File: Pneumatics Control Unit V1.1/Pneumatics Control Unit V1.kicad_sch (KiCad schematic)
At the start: 50 parts, among them J3 RX_PORT, U2 SN65HVD1782D, U3 FT2232D, Y1 Resonator_Small

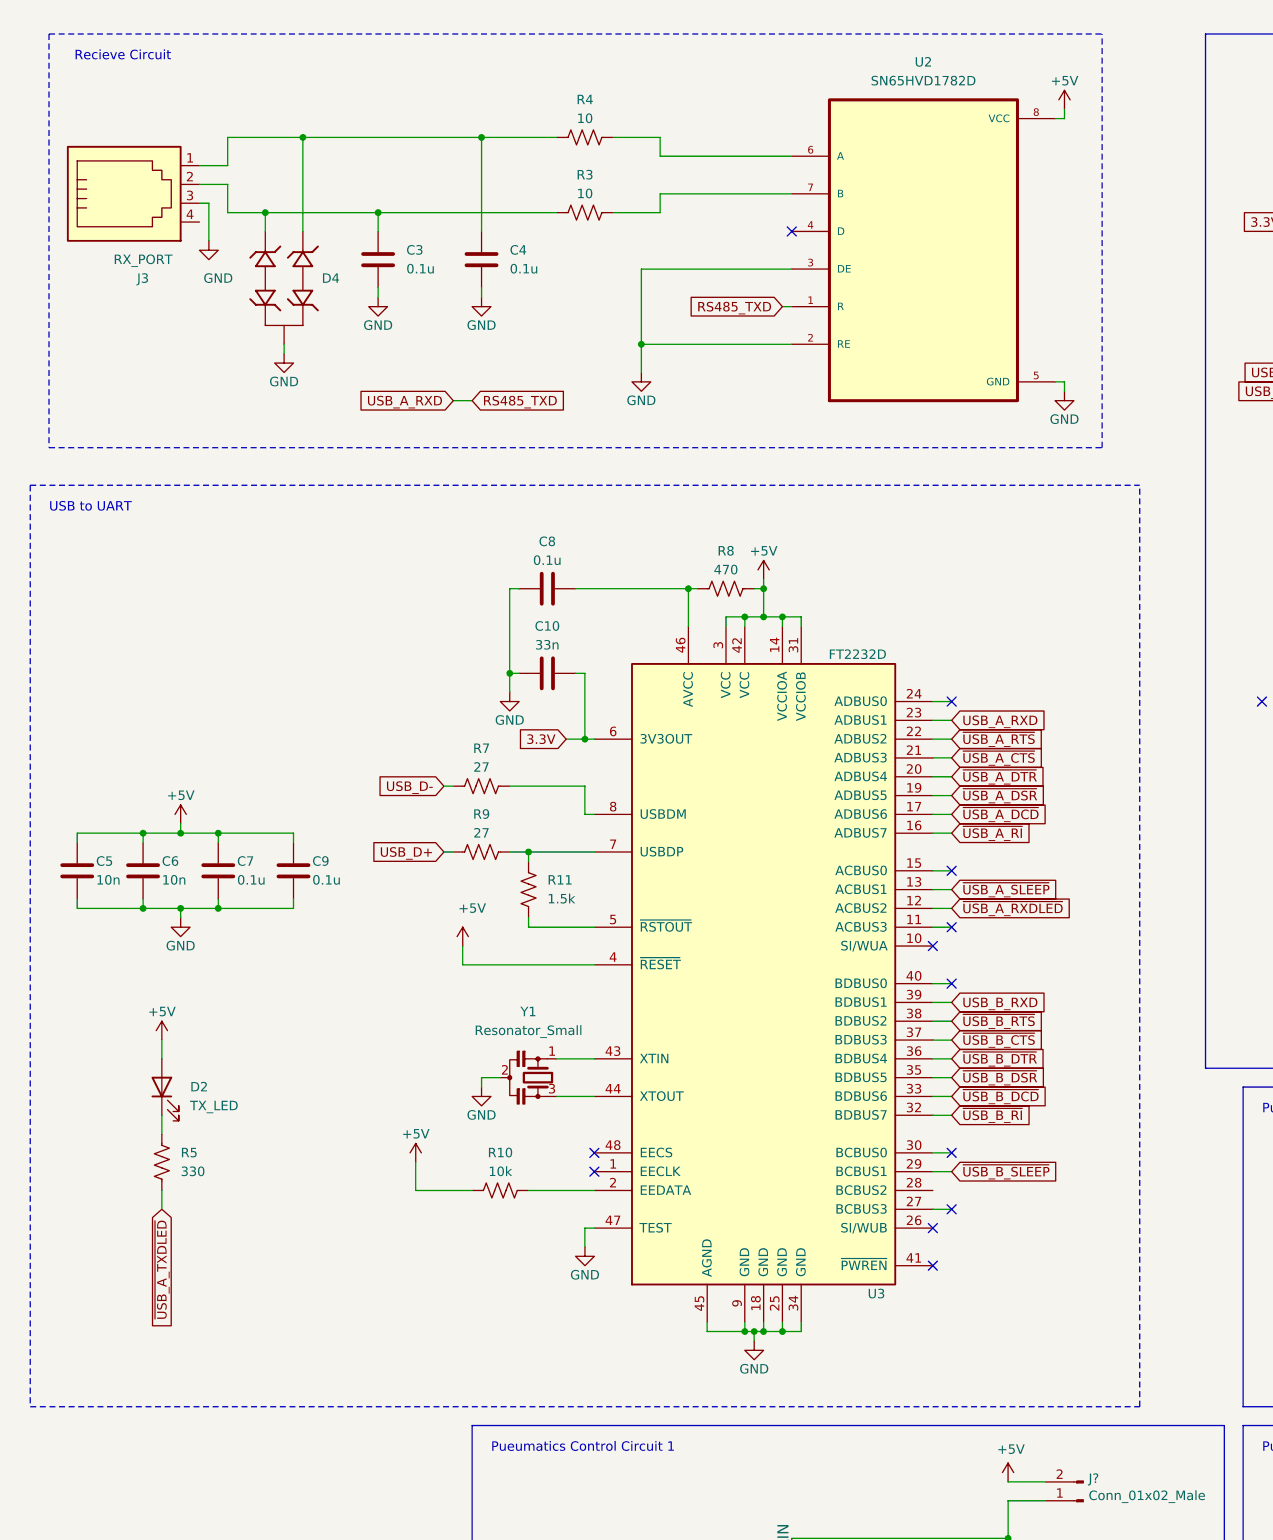
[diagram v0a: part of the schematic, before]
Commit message: using a new chip for RS485 to UART
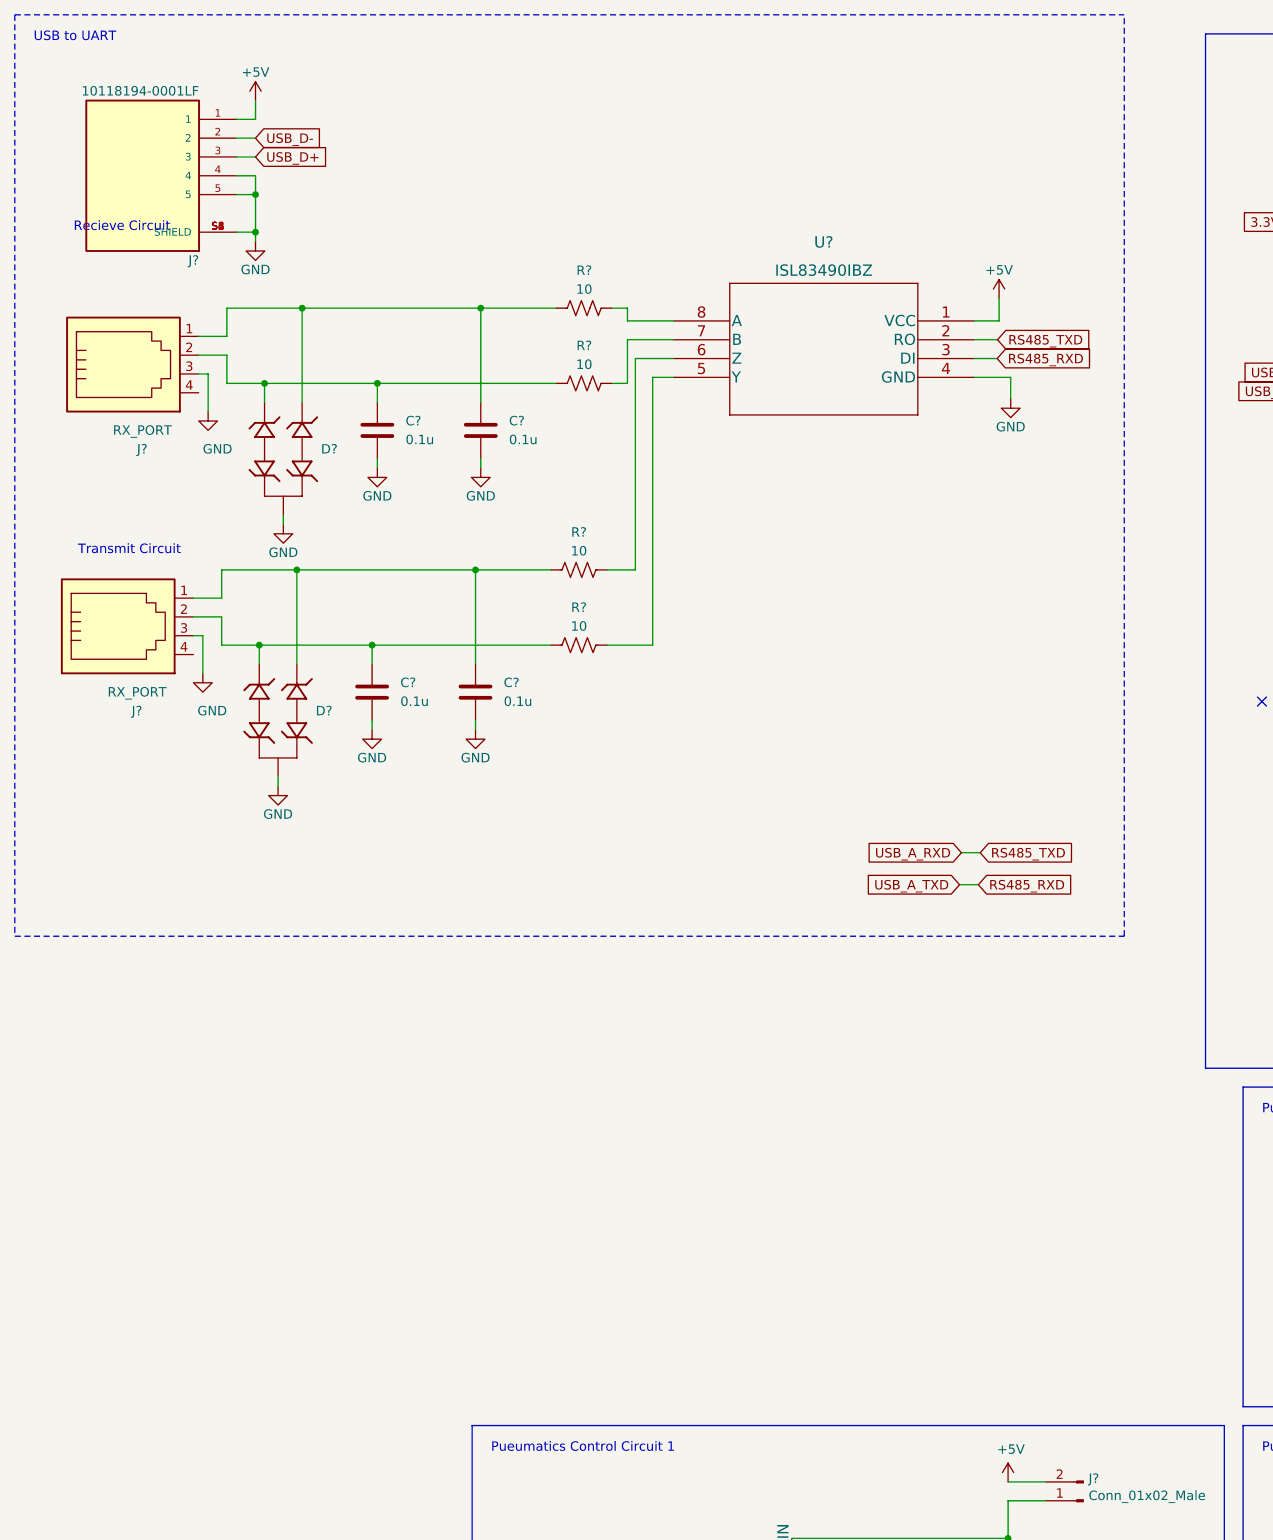
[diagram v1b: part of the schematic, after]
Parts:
- removed C10: 33n, Capacitor_SMD:C_0805_2012Metric_Pad1.18x1.45mm_HandSolder, symbol Device:C
- removed C3, C4, C7, C8, C9: 0.1u, Capacitor_SMD:C_0805_2012Metric_Pad1.18x1.45mm_HandSolder, symbol Device:C
- removed C5, C6: 10n, Capacitor_SMD:C_0805_2012Metric_Pad1.18x1.45mm_HandSolder, symbol Device:C
- removed D2: TX_LED, LED_SMD:LED_0805_2012Metric_Pad1.15x1.40mm_HandSolder, symbol Device:LED
- removed D4: CDSOT23-SM712, CDSOT23-SM712:SOT-23-3, symbol CDSOT23-SM712:CDSOT23-SM712
- removed J3: RX_PORT, Andrew_Custom:C189737, symbol Connector:4P4C
- removed R10: 10k, Resistor_SMD:R_0805_2012Metric_Pad1.20x1.40mm_HandSolder, symbol Device:R_US
- removed R11: 1.5k, Resistor_SMD:R_0805_2012Metric_Pad1.20x1.40mm_HandSolder, symbol Device:R_US
- removed R3, R4: 10, Resistor_SMD:R_0805_2012Metric_Pad1.20x1.40mm_HandSolder, symbol Device:R_US
- removed R5: 330, Resistor_SMD:R_0805_2012Metric_Pad1.20x1.40mm_HandSolder, symbol Device:R_US
- removed R7, R9: 27, Resistor_SMD:R_0805_2012Metric_Pad1.20x1.40mm_HandSolder, symbol Device:R_US
- removed R8: 470, Resistor_SMD:R_0805_2012Metric_Pad1.20x1.40mm_HandSolder, symbol Device:R_US
- removed U2: SN65HVD1782D, SN65HVD1782D:SOIC127P599X175-8N, symbol SN65HVD1782D:SN65HVD1782D
- removed U3: FT2232D, Package_QFP:LQFP-48_7x7mm_P0.5mm, symbol Interface_USB:FT2232D
- removed Y1: Resonator_Small, OSC_CSTCE16M0V53-R0:OSC_CSTCE16M0V53-R0, symbol Device:Resonator_Small
- added C? (x4): 0.1u, Capacitor_SMD:C_0805_2012Metric_Pad1.18x1.45mm_HandSolder, symbol Device:C
- added D? (x2): CDSOT23-SM712, CDSOT23-SM712:SOT-23-3, symbol CDSOT23-SM712:CDSOT23-SM712
- added J? (x2): RX_PORT, Andrew_Custom:C189737, symbol Connector:4P4C
- added J?: 10118194-0001LF, 10118194-0001LF:AMPHENOL_10118194-0001LF, symbol 10118194-0001LF:10118194-0001LF
- added R? (x4): 10, Resistor_SMD:R_0805_2012Metric_Pad1.20x1.40mm_HandSolder, symbol Device:R_US
- added U?: ISL83490IBZ, SOIC8_4X5_INR, symbol 2022-03-23_15-47-26:ISL83490IBZ
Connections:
- net +5V: now also J?.1, U?.1 (VCC)
- net GND: now also C?.2, C?.2, C?.2, C?.2, D?.3, D?.3, J?.3, J?.3, J?.4, J?.5, J?.S1 (SHIELD), J?.S2 (SHIELD), J?.S3 (SHIELD), J?.S4 (SHIELD), J?.S5 (SHIELD), J?.S6 (SHIELD), U?.4 (GND)
- net RS485_TXD: now also U?.2 (RO)
- net USB_D+: now also J?.3
- net USB_D-: now also J?.2
- new net: R?.2, U?.5 (Y)
- new net: R?.2, U?.6 (Z)
- new net: R?.2, U?.7 (B)
- new net: R?.2, U?.8 (A)
- new net: C?.1, D?.2, J?.1, R?.1 (x2)
- new net: C?.1, D?.1, J?.2, R?.1 (x2)
- new net RS485_RXD: U?.3 (DI)
- no-connect marks 56 -> 44
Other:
- note added: "Transmit Circuit"

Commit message: Cleaning up the schematic
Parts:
- removed J?: 10118194-0001LF, 10118194-0001LF:AMPHENOL_10118194-0001LF, symbol 10118194-0001LF:10118194-0001LF
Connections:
- net RS485_RXD: now also J?.17 (TX1)
- net RS485_TXD: now also J?.19 (RX1)
- no-connect marks 44 -> 42
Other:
- note added: "RS485 to UART"
- note removed: "Recieve Circuit"
- note removed: "USB to UART"
- moved on the sheet: C?, D?, H1, H2, H3, J?, MOSFET?, R?, U?

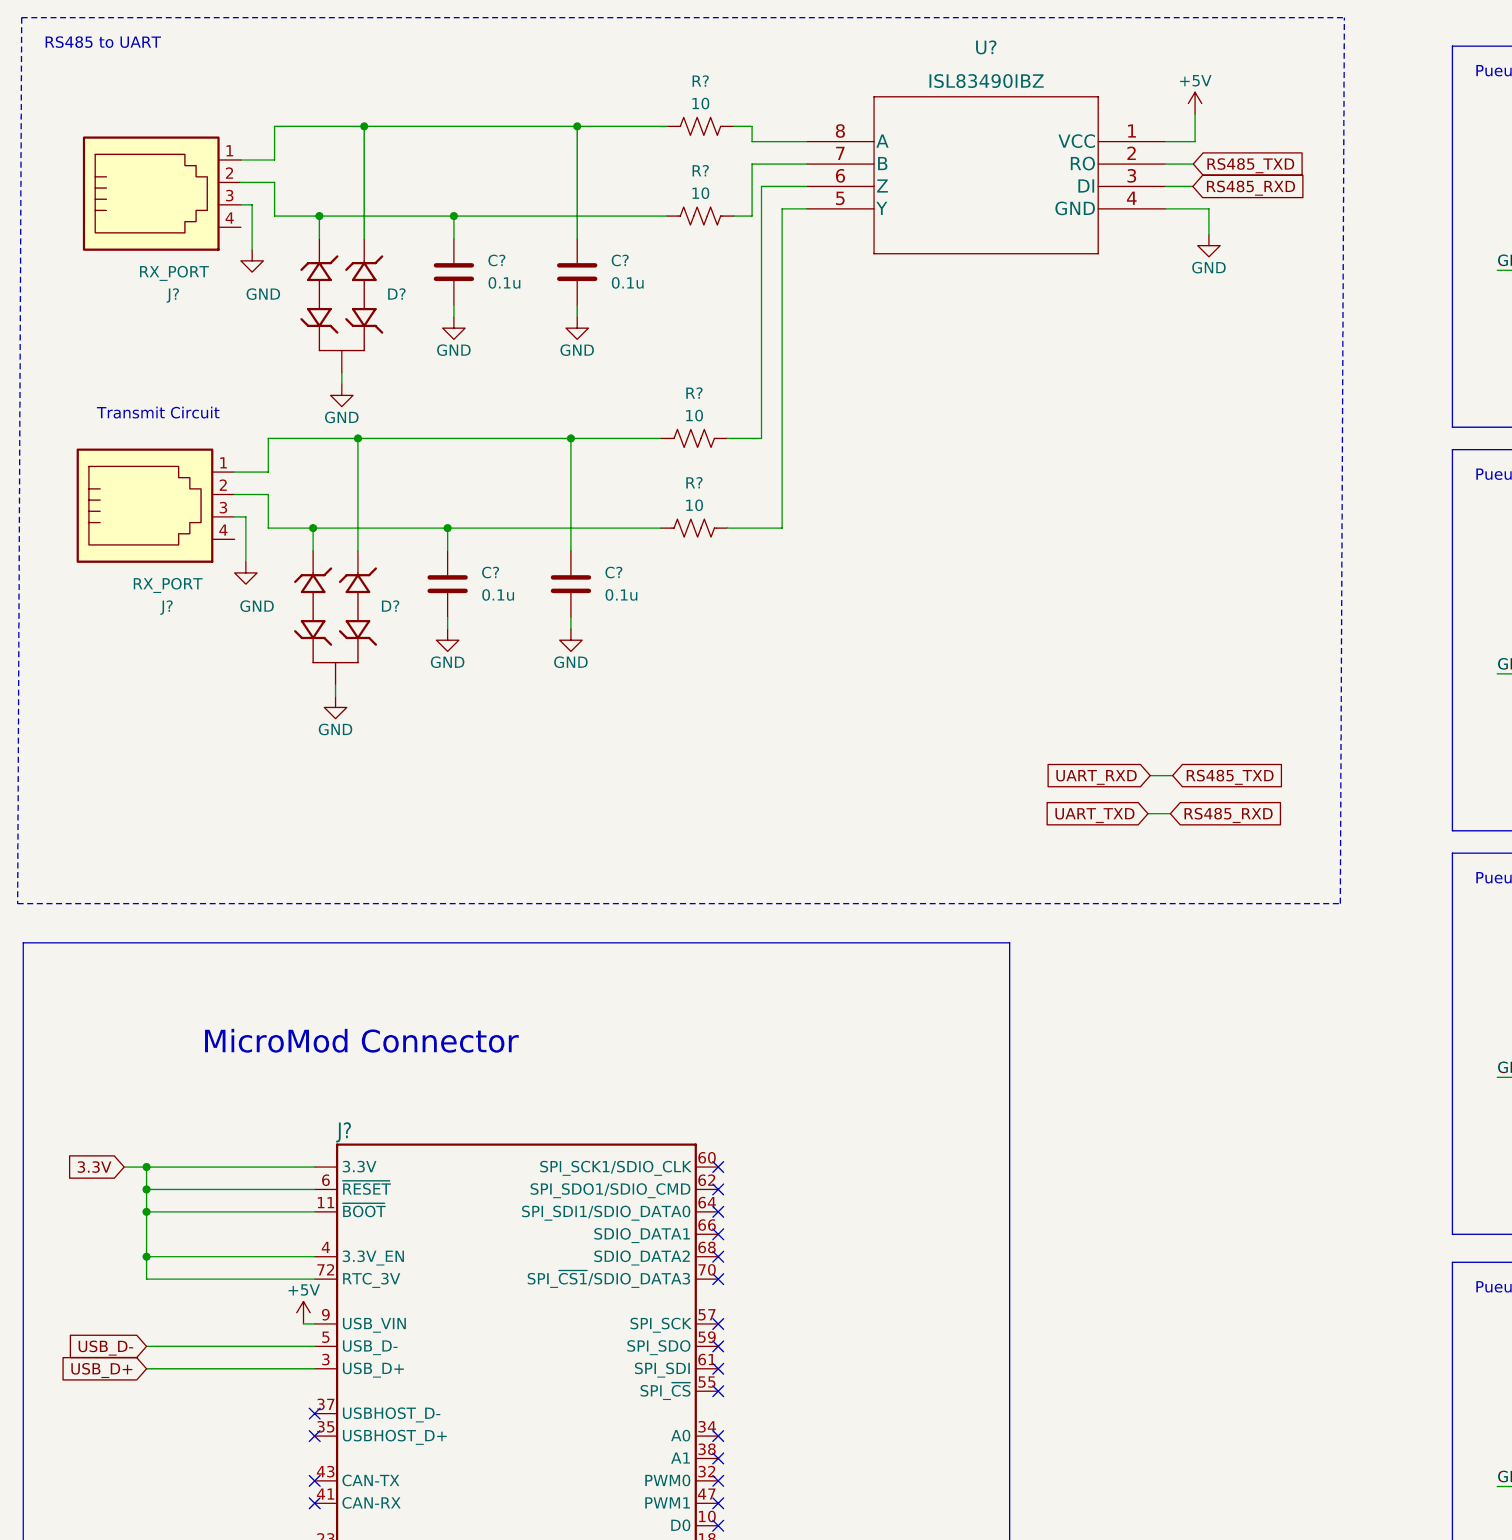
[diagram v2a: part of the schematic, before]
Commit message: Adding voltage converters
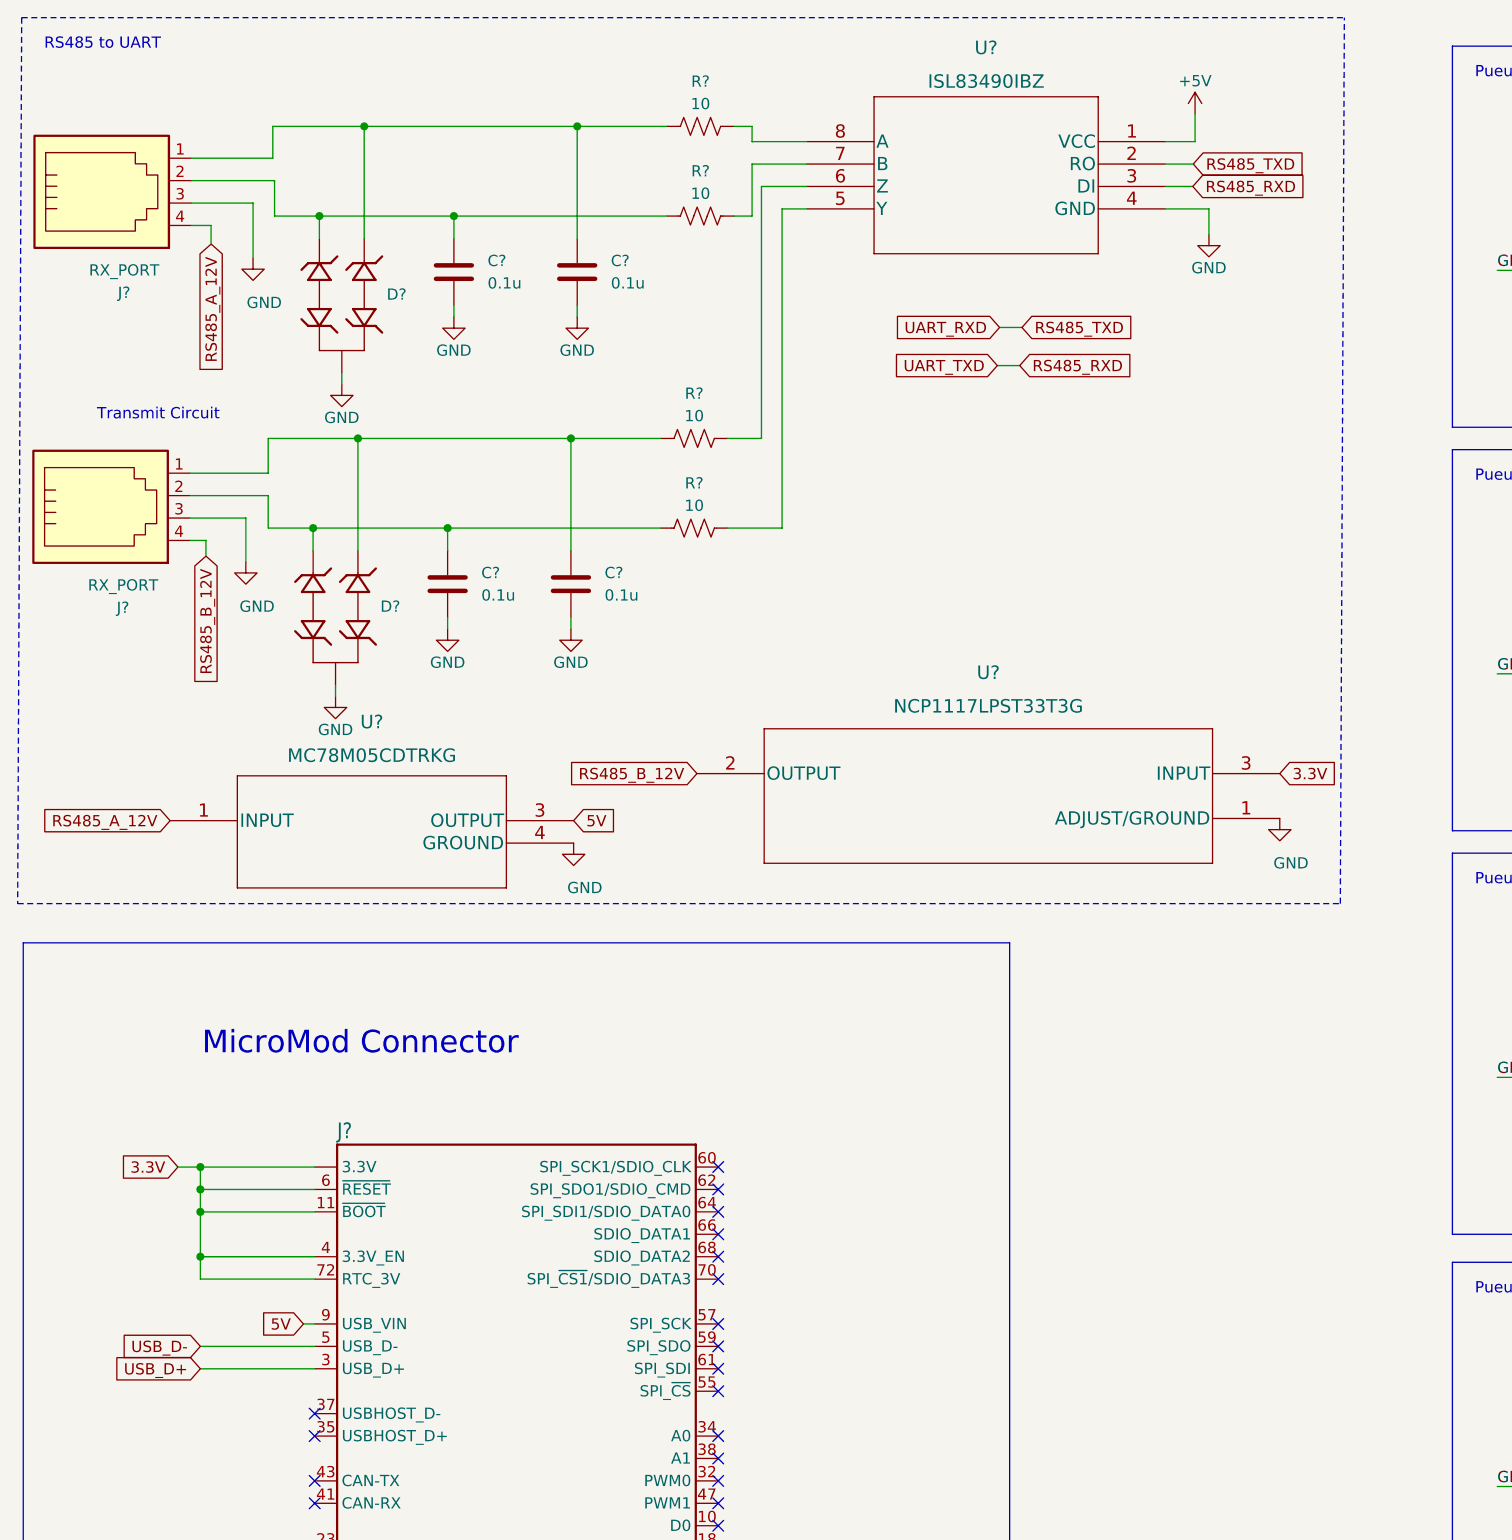
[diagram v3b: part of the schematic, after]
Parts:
- added U?: NCP1117LPST33T3G, SOT223-3_ONS, symbol 3.3:NCP1117LPST33T3G
- added U?: MC78M05CDTRKG, DPAK-3_ONS, symbol 2022-03-25_21-05-18:MC78M05CDTRKG
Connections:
- net +5V: no longer J?.9 (USB_VIN)
- net 3.3V: now also U?.3 (INPUT)
- net GND: now also U?.1 (ADJUST/GROUND), U?.4 (GROUND)
- net RS485_B_12V: now reaches J?.4
- net RS485_B_12V: now also U?.2 (OUTPUT)
- net RS485_A_12V: now reaches J?.4
- net RS485_A_12V: now also U?.1 (INPUT)
- new net 5V: J?.9 (USB_VIN), U?.3 (OUTPUT)
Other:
- moved on the sheet: J?
